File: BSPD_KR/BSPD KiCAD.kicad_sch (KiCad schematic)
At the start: 71 parts, among them J1 Conn_01x03, J3 Conn_01x02, J89 Conn_01x02, K1 G5Q-1A4-DC12, Q1 2N7000, Q2 2N7000, U1 LM741CN/NOPB, U18 SN74AHCT1G08DBVR, U19 LM339N, U2 LM741CN/NOPB, U3 LM741CN/NOPB, U4 LM7805MPX/NOPB, U5 LM339N, U6 SN74AHC1G02DBVR, U9 SN74LVC1G04DBVT

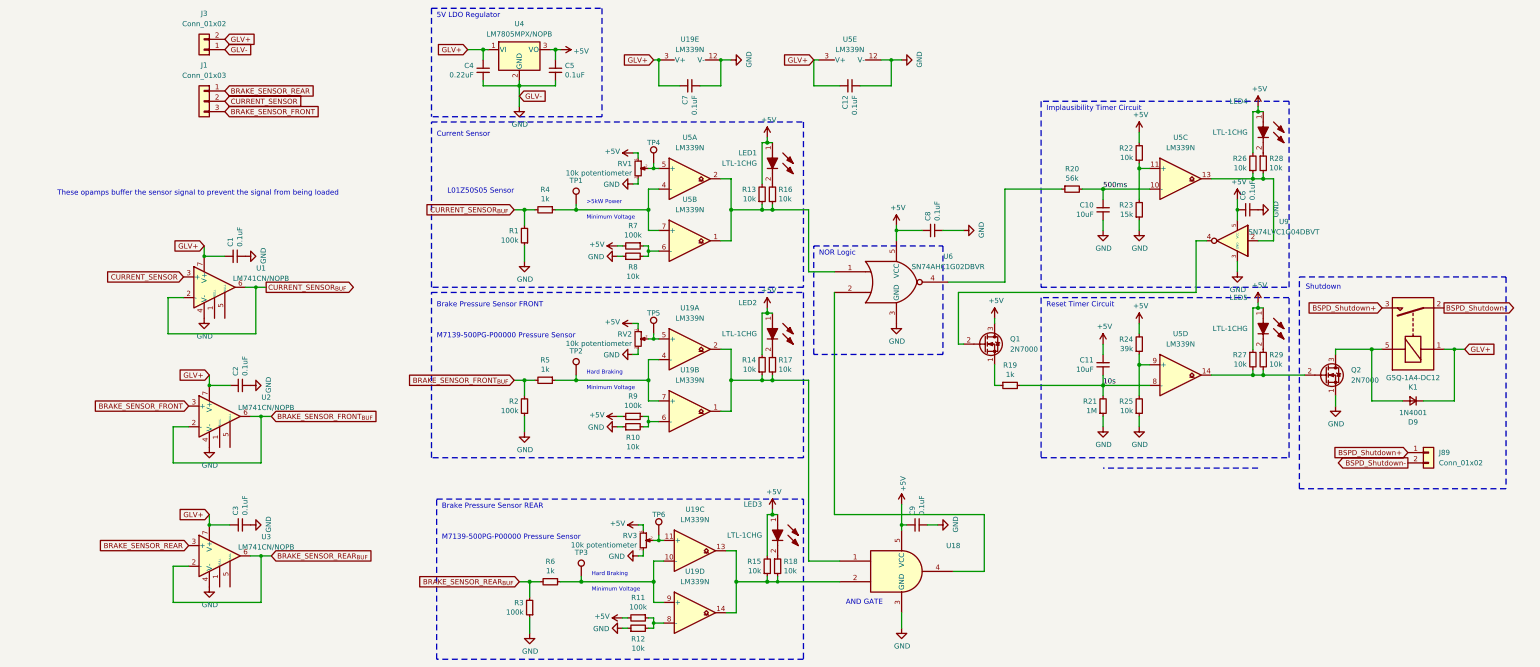
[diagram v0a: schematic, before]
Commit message: Slave with SMD and no other fuses
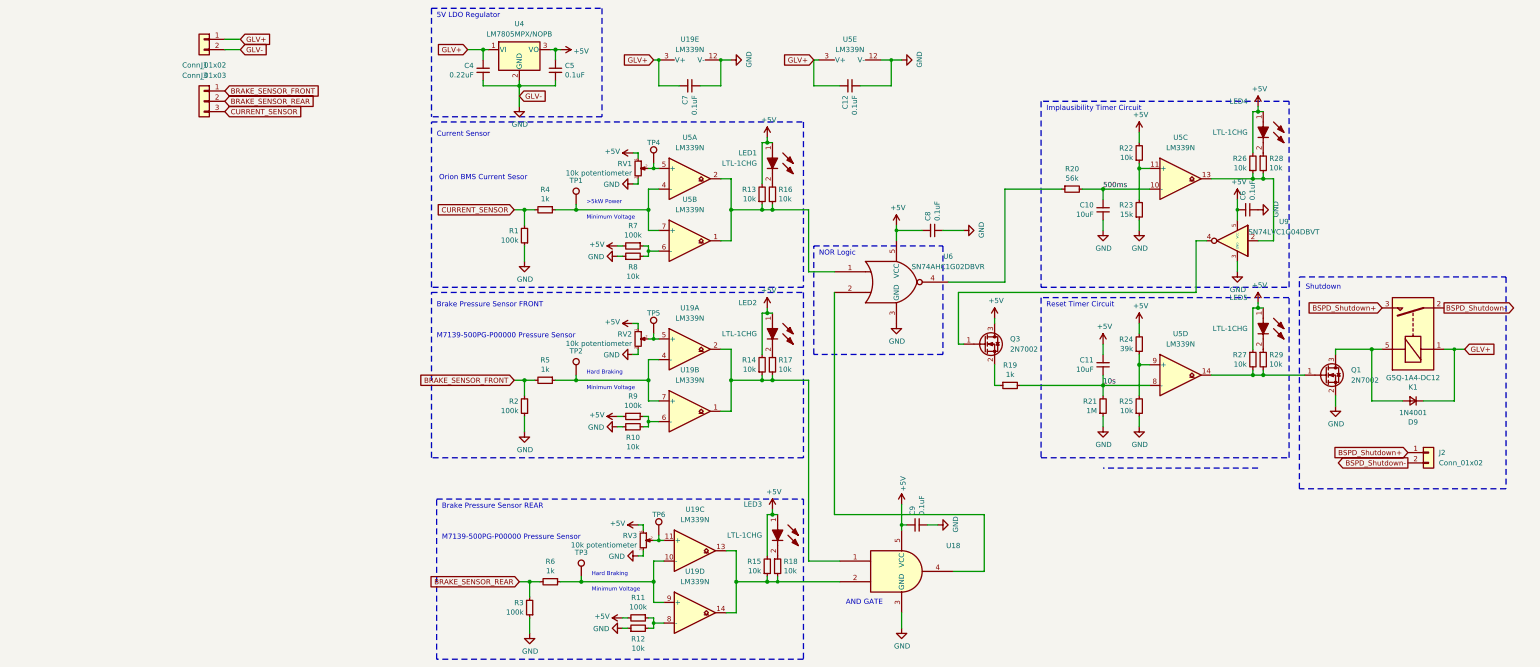
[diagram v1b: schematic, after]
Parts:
- removed C1, C2, C3: 0.1uF, FA14_Capacitor:FA18X7R1H104KNU00, symbol Device:C_Small
- removed Q1, Q2: 2N7000, Package_TO_SOT_THT:TO-92_Inline, symbol Transistor_FET:2N7000
- removed U1, U2, U3: LM741CN/NOPB, Package_DIP:DIP-8_W7.62mm, symbol Amplifier_Operational:LM741
- added Q1, Q3: 2N7002, Package_TO_SOT_SMD:SOT-23, symbol Transistor_FET:2N7002
- C12, C5, C6, C7, C8, C9: footprint FA14_Capacitor:FA18X7R1H104KNU00 -> Kicad_Libraries:FA18X7R1H104KNU00
- C4: footprint FA14_Capacitor:FA14X7R1H224KNU00 -> Kicad_Libraries:FA14X7R1H224KNU00
- LED1, LED2, LED3, LED4, LED5: footprint LTL1CHG:LTL1CHG -> Kicad_Libraries:LTL1CHG
- U19, U5: footprint LM339N:DIP794W53P254L1930H508Q14N -> Kicad_Libraries:DIP794W53P254L1930H508Q14N
- renumbered J89 to J2
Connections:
- net BRAKE_SENSOR_FRONT_{BUF} is gone; now on net BRAKE_SENSOR_FRONT: R2.2, R5.2
- net BRAKE_SENSOR_REAR_{BUF} is gone; now on net BRAKE_SENSOR_REAR: R3.2, R6.2
- net CURRENT_SENSOR_{BUF} is gone; now on net CURRENT_SENSOR: R1.2, R4.2
- net +5V: now also Q3.3 (D)
- net BRAKE_SENSOR_FRONT: now also J1.1 (Pin_1); no longer J1.3 (Pin_3)
- net BRAKE_SENSOR_REAR: now also J1.2 (Pin_2); no longer J1.1 (Pin_1)
- net CURRENT_SENSOR: now also J1.3 (Pin_3); no longer J1.2 (Pin_2)
- net GLV+: now also J3.1 (Pin_1); no longer J3.2 (Pin_2)
- net GND: now also J3.2 (Pin_2), Q1.2 (S); no longer J3.1 (Pin_1)
- net at R19.1: now also Q3.2 (S)
- net at D9.2 (A), K1.5: now also Q1.3 (D)
- net at R27.2, R29.2, U5.14: now also Q1.1 (G)
- net at U9.4: now also Q3.1 (G)
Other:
- note added: "Orion BMS Current Sesor"
- note removed: "L01Z50S05 Sensor"
- note removed: "These opamps buffer the sensor signal to prevent the signal from being loaded"
- moved on the sheet: J3
